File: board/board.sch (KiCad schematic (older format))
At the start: 13 parts

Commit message: Pushing for Kicad reinstall
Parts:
- removed R? (x2): 10k, symbol Device:R_Small
- added C11: 2u2, symbol Device:C_Small
- added C3, C5: 12p, symbol Device:C_Small
- added R1: 47, symbol Device:R_Small_US
- added R2, R3, R6: 0, symbol Device:R_Small_US
- added R4, R5: 10k, symbol Device:R_Small_US
- added U2: MP2359, Package_TO_SOT_SMD:SOT-23-6, symbol custom:MP2359
- added Y1: 16MHz, symbol Device:Crystal_GND24_Small
- gave numbers to parts that had none: 11
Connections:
- net labels added: BUCK_EN, BUCK_IN, BUCK_SW
- wire segments 55 -> 79

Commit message: Small update on power section
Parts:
- added C?: 10u, Capacitor_SMD:C_0603_1608Metric, symbol Device:C_Small
- added C?: 10n, Capacitor_SMD:C_0603_1608Metric, symbol Device:C_Small
- added C? (x2): 2u2, Capacitor_SMD:C_0603_1608Metric, symbol Device:C_Small
- added D?: B5819W, symbol Device:D_Schottky_Small
- added F?: 400mA, symbol Device:Polyfuse_Small
- added FB?: 600 @ 100 MHz, symbol Device:Ferrite_Bead_Small
- added L?: 10u, symbol Device:L_Small
- added Q?: AO3401A, Package_TO_SOT_SMD:SOT-23, symbol Transistor_FET:AO3401A
- added R?: 100k, Resistor_SMD:R_0603_1608Metric, symbol Device:R_Small_US
- added R?: 68k, Resistor_SMD:R_0603_1608Metric, symbol Device:R_Small_US
- added R?: 47k, Resistor_SMD:R_0603_1608Metric, symbol Device:R_Small_US
- added R?: 15k, Resistor_SMD:R_0603_1608Metric, symbol Device:R_Small_US
- added R?: 270, Resistor_SMD:R_0603_1608Metric, symbol Device:R_Small_US
- C1, C11, C8, C9: footprint (none) -> Capacitor_SMD:C_0603_1608Metric
- C10, C12, C2, C3, C4, C5, C6, C7: footprint (none) -> Capacitor_SMD:C_0402_1005Metric
- R1: footprint (none) -> Resistor_SMD:R_0402_1005Metric
- R2, R3, R4, R5, R6: footprint (none) -> Resistor_SMD:R_0603_1608Metric
- U2: symbol custom:MP2359 -> board-rescue:MP2359-custom
- Y1: footprint (none) -> Crystal:Crystal_SMD_3225-4Pin_3.2x2.5mm
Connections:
- net labels added: +12V, BUCK_BST, BUCK_FB
- wire segments 79 -> 111
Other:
- note added: "Under construction"
- moved on the sheet: C12, R4, R5, R6, U3

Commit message: quick push
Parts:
- added D?: D_Zener_Small, symbol Device:D_Zener_Small
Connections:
- net labels added: VCC
- wire segments 111 -> 112
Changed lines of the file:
@@
 $EndComp
 Wire Wire Line
-	7900 3450 8200 3450
+	7900 3450 8000 3450
 $Comp
 L Device:C_Small C?
@@
 Text Notes 7200 7000 0    247  ~ 49
 Under construction
+$Comp
+L Device:D_Zener_Small D?
+U 1 1 6090273B
+P 8000 3350
+F 0 "D?" V 8046 3280 50  0000 R CNN
+F 1 "D_Zener_Small" V 7955 3280 50  0000 R CNN
+F 2 "" V 8000 3350 50  0001 C CNN
+F 3 "~" V 8000 3350 50  0001 C CNN
+	1    8000 3350
+	0    -1   -1   0
+$EndComp
+Connection ~ 8000 3450
+Wire Wire Line
+	8000 3450 8200 3450
+$Comp
+L power:VCC #PWR?
+U 1 1 60903D35
+P 8000 3250
+F 0 "#PWR?" H 8000 3100 50  0001 C CNN
+F 1 "VCC" H 8015 3423 50  0000 C CNN
+F 2 "" H 8000 3250 50  0001 C CNN
+F 3 "" H 8000 3250 50  0001 C CNN
+	1    8000 3250
+	1    0    0    -1
+$EndComp
 $EndSCHEMATC

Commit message: Updated board schematic
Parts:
- removed D?: D_Zener_Small, symbol Device:D_Zener_Small
- removed R2, R3: 0, Resistor_SMD:R_0603_1608Metric, symbol Device:R_Small_US
- added C?: 1u, Capacitor_SMD:C_0402_1005Metric, symbol Device:C_Small
- added C?: 10n, Capacitor_SMD:C_0402_1005Metric, symbol Device:C_Small
- added D1: D_Schottky_Small, symbol Device:D_Schottky_Small
- added FB?: 600 @ 100 MHz, symbol Device:Ferrite_Bead_Small
- added J1: USB_B_Micro, symbol Connector:USB_B_Micro
- added U4: USBLC6-2SC6, Package_TO_SOT_SMD:SOT-23-6, symbol Power_Protection:USBLC6-2SC6
- F1: renamed from F?; value 400mA -> 300mA
- gave numbers to parts that had none: 13
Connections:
- net labels added: USB_CONN_D+, USB_CONN_D-, USB_D+, USB_D-, VBUS
- net labels removed: VCC
- wire segments 112 -> 107
- no-connect marks 0 -> 2
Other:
- note added: "DCDC"
- note added: "Ext. Flash"
- note added: "MCU Decoupling"
- note added: "Power ORing\n"
- note added: "USB"
- moved on the sheet: C11, C13, C14, C15, C16, C3, C5, C8, C9, D2, F1, FB1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

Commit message: Updated board
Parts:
- added D3: POW LED [Gr], LED_SMD:LED_0603_1608Metric, symbol Device:LED_Small
- added R12: 1.5k, Resistor_SMD:R_0603_1608Metric, symbol Device:R_Small_US
- D1, D2: footprint (none) -> Diode_SMD:D_0603_1608Metric
- F1: footprint (none) -> Fuse:Fuse_1206_3216Metric
- FB1, L1: footprint (none) -> Inductor_SMD:L_0603_1608Metric
- FB2: renamed from FB?; footprint (none) -> Inductor_SMD:L_0603_1608Metric
- J1: footprint (none) -> Connector_USB:USB_Micro-B_Amphenol_10103594-0001LF_Horizontal; symbol Connector:USB_B_Micro -> board-rescue:USB_B_Micro-Connector
- gave numbers to parts that had none: 2
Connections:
- net labels added: SPI3_!CS, SPI3_MISO, SPI3_MOSI, SPI3_SCLK, TIM1_CH1
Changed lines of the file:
@@
 $Descr A4 11693 8268
 encoding utf-8
-Sheet 1 1
+Sheet 1 3
 Title ""
 Date ""
@@
 F 0 "F1" V 8400 3550 50  0000 C CNN
 F 1 "300mA" V 8600 3550 50  0000 C CNN
-F 2 "" H 8550 3350 50  0001 L CNN
+F 2 "Fuse:Fuse_1206_3216Metric" H 8550 3350 50  0001 L CNN
 F 3 "~" H 8500 3550 50  0001 C CNN
 	1    8500 3550
@@
 F 0 "FB1" V 8900 3650 50  0000 C CNN
 F 1 "600 @ 100 MHz" V 8650 3750 50  0000 C CNN
-F 2 "" V 8730 3550 50  0001 C CNN
+F 2 "Inductor_SMD:L_0603_1608Metric" V 8730 3550 50  0001 C CNN
 F 3 "~" H 8800 3550 50  0001 C CNN
 	1    8800 3550
@@
 F 0 "D2" V 9700 5500 50  0000 L CNN
 F 1 "B5819W" V 9800 5500 50  0000 L CNN
-F 2 "" V 9750 5850 50  0001 C CNN
+F 2 "Diode_SMD:D_0603_1608Metric" V 9750 5850 50  0001 C CNN
 F 3 "~" V 9750 5850 50  0001 C CNN
 	1    9750 5850
@@
 F 0 "L1" V 10050 5650 50  0000 C CNN
 F 1 "10u" V 9900 5650 50  0000 C CNN
-F 2 "" H 9950 5650 50  0001 C CNN
+F 2 "Inductor_SMD:L_0603_1608Metric" H 9950 5650 50  0001 C CNN
 F 3 "~" H 9950 5650 50  0001 C CNN
 	1    9950 5650
@@
 F 0 "D1" V 8296 3230 50  0000 R CNN
 F 1 "D_Schottky_Small" V 8400 3250 50  0000 R CNN
-F 2 "" V 8250 3300 50  0001 C CNN
+F 2 "Diode_SMD:D_0603_1608Metric" V 8250 3300 50  0001 C CNN
 F 3 "~" V 8250 3300 50  0001 C CNN
 	1    8250 3300
@@
 	8900 3550 9150 3550
 $Comp
-L Connector:USB_B_Micro J1
+L board-rescue:USB_B_Micro-Connector J1
 U 1 1 609103DF
 P 5850 6900
 F 0 "J1" H 5907 7367 50  0000 C CNN
 F 1 "USB_B_Micro" H 5907 7276 50  0000 C CNN
-F 2 "" H 6000 6850 50  0001 C CNN
+F 2 "Connector_USB:USB_Micro-B_Amphenol_10103594-0001LF_Horizontal" H 6000 6850 50  0001 C CNN
 F 3 "~" H 6000 6850 50  0001 C CNN
 	1    5850 6900
@@
 Power ORing\n
 $Comp
-L Device:Ferrite_Bead_Small FB?
+L Device:Ferrite_Bead_Small FB2
 U 1 1 60A20CBB
 P 4050 950
-F 0 "FB?" V 4150 850 50  0000 C CNN
+F 0 "FB2" V 4150 850 50  0000 C CNN
 F 1 "600 @ 100 MHz" V 4250 900 50  0000 C CNN
-F 2 "" V 3980 950 50  0001 C CNN
+F 2 "Inductor_SMD:L_0603_1608Metric" V 3980 950 50  0001 C CNN
 F 3 "~" H 4050 950 50  0001 C CNN
 	1    4050 950
@@
 $EndComp
 $Comp
-L Device:C_Small C?
+L Device:C_Small C17
 U 1 1 60A21654
 P 4350 1050
-F 0 "C?" H 4442 1096 50  0000 L CNN
+F 0 "C17" H 4442 1096 50  0000 L CNN
 F 1 "1u" H 4442 1005 50  0000 L CNN
 F 2 "Capacitor_SMD:C_0402_1005Metric" H 4350 1050 50  0001 C CNN
@@
 $EndComp
 $Comp
-L power:+3V3 #PWR?
+L power:+3V3 #PWR06
 U 1 1 60A21B51
 P 3800 950
-F 0 "#PWR?" H 3800 800 50  0001 C CNN
+F 0 "#PWR06" H 3800 800 50  0001 C CNN
 F 1 "+3V3" H 3815 1123 50  0000 C CNN
 F 2 "" H 3800 950 50  0001 C CNN
@@
 	3950 950  3800 950
 $Comp
-L Device:C_Small C?
+L Device:C_Small C18
 U 1 1 60A25BB7
 P 4750 1050
-F 0 "C?" H 4842 1096 50  0000 L CNN
+F 0 "C18" H 4842 1096 50  0000 L CNN
 F 1 "10n" H 4842 1005 50  0000 L CNN
 F 2 "Capacitor_SMD:C_0402_1005Metric" H 4750 1050 50  0001 C CNN
@@
 $EndComp
 $Comp
-L power:+3.3VA #PWR?
+L power:+3.3VA #PWR08
 U 1 1 60A2600F
 P 4750 850
-F 0 "#PWR?" H 4750 700 50  0001 C CNN
+F 0 "#PWR08" H 4750 700 50  0001 C CNN
 F 1 "+3.3VA" H 4765 1023 50  0000 C CNN
 F 2 "" H 4750 850 50  0001 C CNN
@@
 Connection ~ 4350 950
 $Comp
-L power:GND #PWR?
+L power:GND #PWR07
 U 1 1 60A2FFCD
 P 4350 1150
-F 0 "#PWR?" H 4350 900 50  0001 C CNN
+F 0 "#PWR07" H 4350 900 50  0001 C CNN
 F 1 "GND" H 4355 977 50  0000 C CNN
 F 2 "" H 4350 1150 50  0001 C CNN
@@
 $EndComp
 $Comp
-L power:GND #PWR?
+L power:GND #PWR09
 U 1 1 60A3071E
 P 4750 1150
-F 0 "#PWR?" H 4750 900 50  0001 C CNN
+F 0 "#PWR09" H 4750 900 50  0001 C CNN
 F 1 "GND" H 4755 977 50  0000 C CNN
 F 2 "" H 4750 1150 50  0001 C CNN
@@
 	1    0    0    -1
 $EndComp
+$Sheet
+S 1400 -1250 1250 900
+U 609AD7E8
+F0 "Sheet609AD7E7" 50
+F1 "sensors.sch" 50
+$EndSheet
+Text GLabel 4650 4350 2    50   Input ~ 0
+TIM1_CH1
+$Sheet
+S 2950 -1250 1300 900
+U 609E7CAF
+F0 "Sheet609E7CAE" 50
+F1 "connectors.sch" 50
+$EndSheet
+$Comp
+L power:+3V3 #PWR010
+U 1 1 609E9B02
+P 7400 5500
+F 0 "#PWR010" H 7400 5350 50  0001 C CNN
+F 1 "+3V3" H 7415 5673 50  0000 C CNN
+F 2 "" H 7400 5500 50  0001 C CNN
+F 3 "" H 7400 5500 50  0001 C CNN
+	1    7400 5500
+	1    0    0    -1
+$EndComp
+$Comp
+L power:GND #PWR011
+U 1 1 609EAD75
+P 7400 5900
+F 0 "#PWR011" H 7400 5650 50  0001 C CNN
+F 1 "GND" H 7405 5727 50  0000 C CNN
+F 2 "" H 7400 5900 50  0001 C CNN
+F 3 "" H 7400 5900 50  0001 C CNN
+	1    7400 5900
+	1    0    0    -1
+$EndComp
+$Comp
+L Device:R_Small_US R12
+U 1 1 609EB0ED
+P 7400 5800
+F 0 "R12" V 7300 5850 50  0000 C CNN
+F 1 "1.5k" V 7500 5850 50  0000 C CNN
+F 2 "Resistor_SMD:R_0603_1608Metric" H 7400 5800 50  0001 C CNN
+F 3 "~" H 7400 5800 50  0001 C CNN
+	1    7400 5800
+	-1   0    0    1
+$EndComp
+$Comp
+L Device:LED_Small D3
+U 1 1 609EF0AE
+P 7400 5600
+F 0 "D3" V 7446 5530 50  0000 R CNN
+F 1 "POW LED [Gr]" V 7355 5530 50  0000 R CNN
+F 2 "LED_SMD:LED_0603_1608Metric" V 7400 5600 50  0001 C CNN
+F 3 "~" V 7400 5600 50  0001 C CNN
+	1    7400 5600
+	0    -1   -1   0
+$EndComp
+Text GLabel 4750 4050 2    50   Input ~ 0
+SPI3_!CS
+Text GLabel 4750 3950 2    50   Input ~ 0
+SPI3_SCLK
+Text GLabel 4750 3850 2    50   Input ~ 0
+SPI3_MOSI
+Text GLabel 4750 3750 2    50   Input ~ 0
+SPI3_MISO
 $EndSCHEMATC

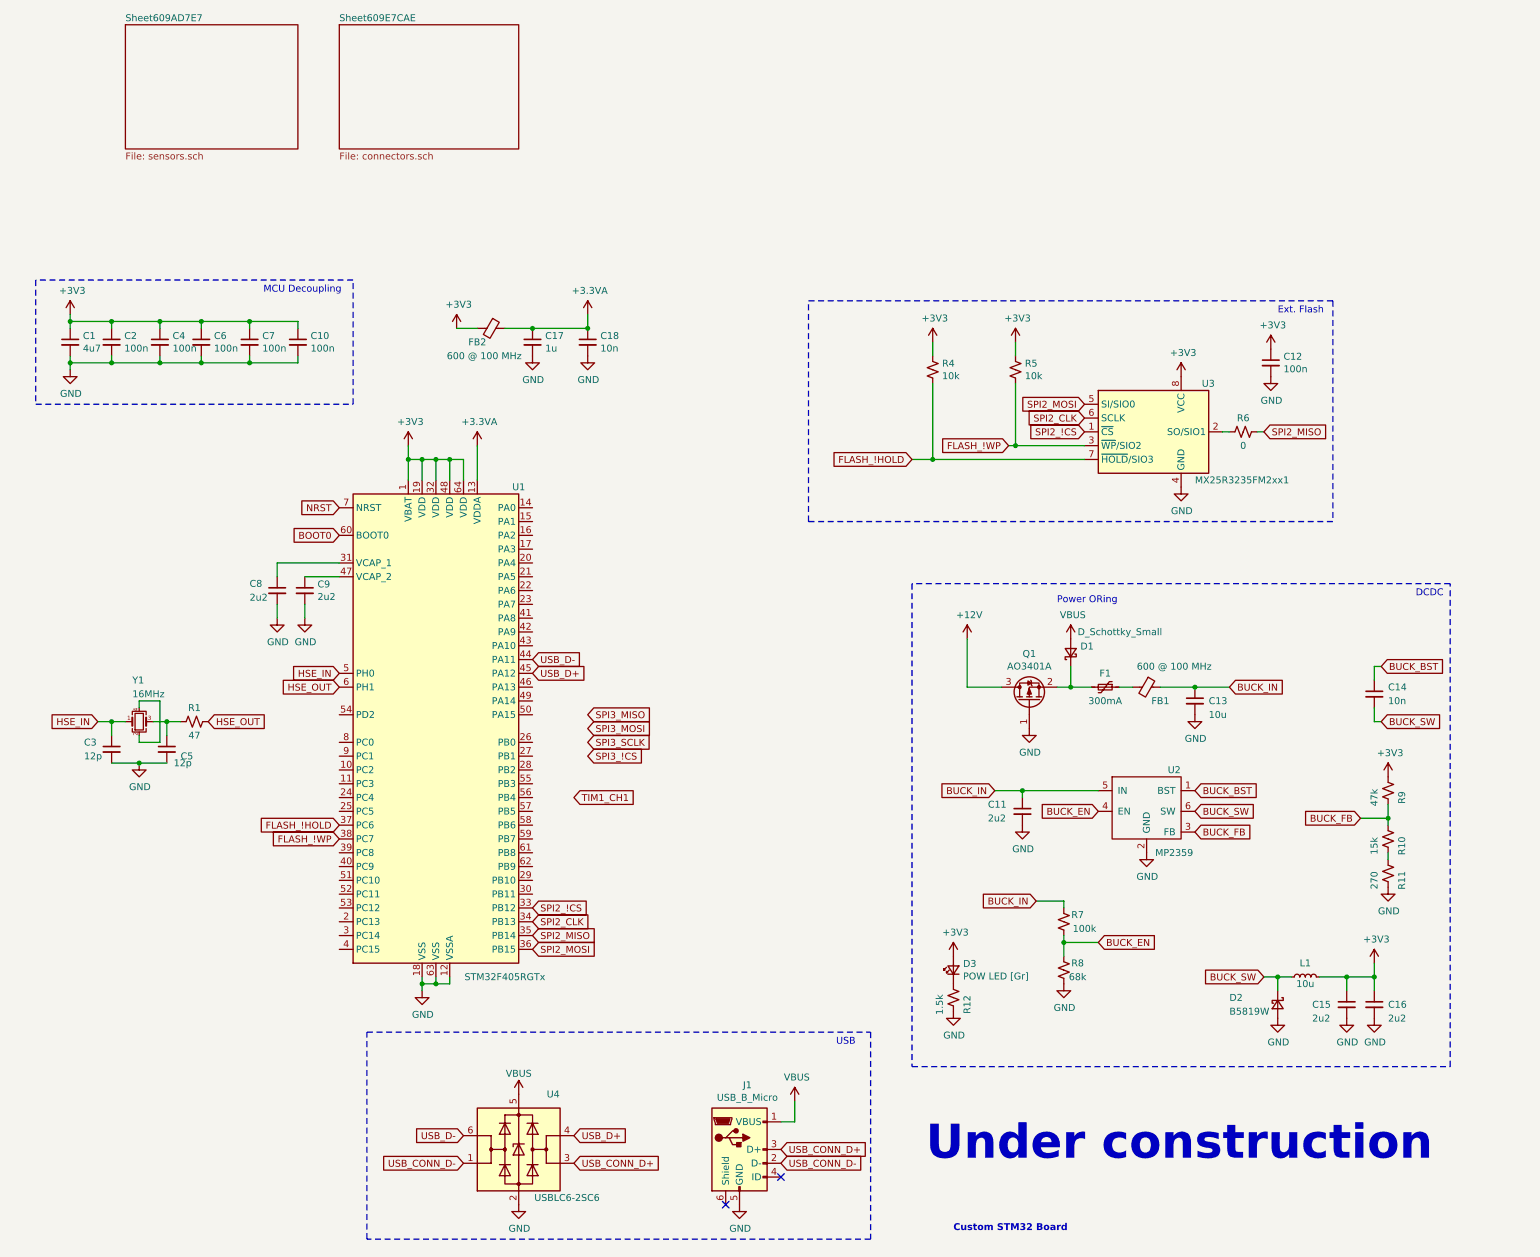
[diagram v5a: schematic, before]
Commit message: Rework on power supply and added pressure sensor
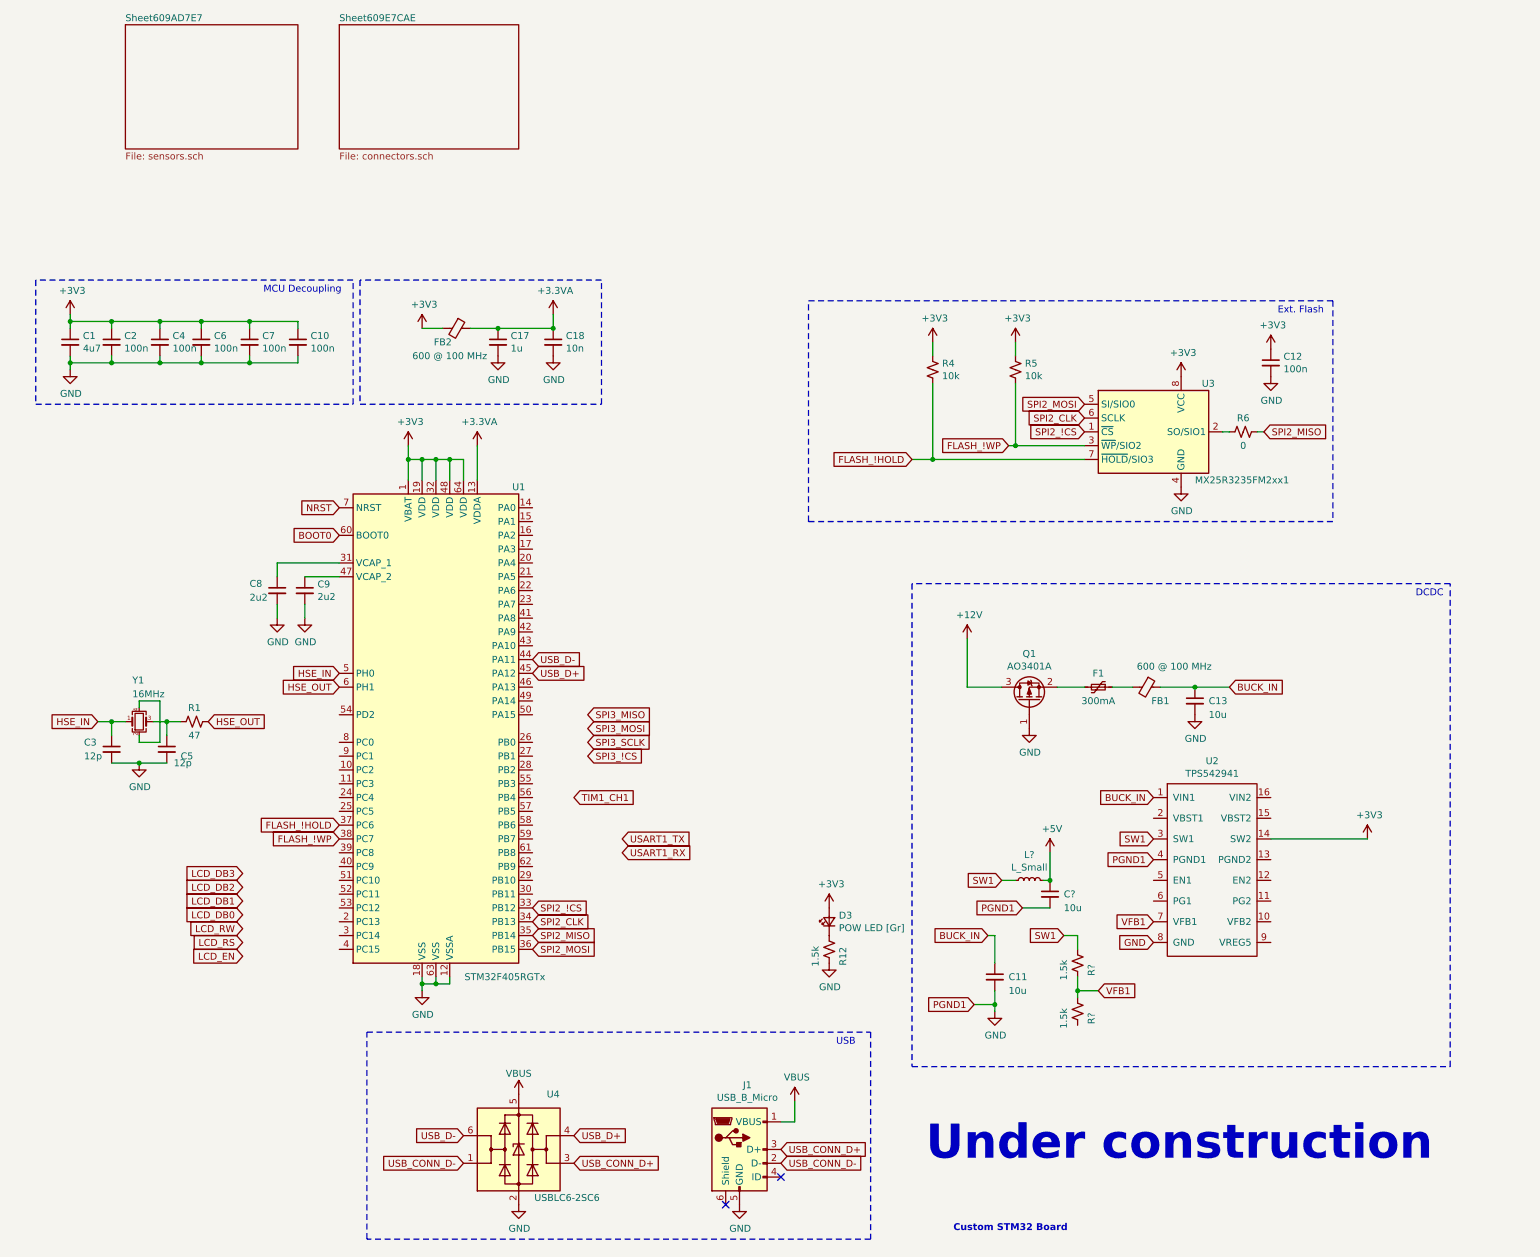
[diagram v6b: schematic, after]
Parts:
- removed C14: 10n, Capacitor_SMD:C_0603_1608Metric, symbol Device:C_Small
- removed C15, C16: 2u2, Capacitor_SMD:C_0603_1608Metric, symbol Device:C_Small
- removed D1: D_Schottky_Small, Diode_SMD:D_0603_1608Metric, symbol Device:D_Schottky_Small
- removed D2: B5819W, Diode_SMD:D_0603_1608Metric, symbol Device:D_Schottky_Small
- removed L1: 10u, Inductor_SMD:L_0603_1608Metric, symbol Device:L_Small
- removed R10: 15k, Resistor_SMD:R_0603_1608Metric, symbol Device:R_Small_US
- removed R11: 270, Resistor_SMD:R_0603_1608Metric, symbol Device:R_Small_US
- removed R7: 100k, Resistor_SMD:R_0603_1608Metric, symbol Device:R_Small_US
- removed R8: 68k, Resistor_SMD:R_0603_1608Metric, symbol Device:R_Small_US
- removed R9: 47k, Resistor_SMD:R_0603_1608Metric, symbol Device:R_Small_US
- removed U2: MP2359, Package_TO_SOT_SMD:SOT-23-6, symbol board-rescue:MP2359-custom
- added C?: 10u, Capacitor_SMD:C_0603_1608Metric, symbol Device:C_Small
- added L?: L_Small, symbol Device:L_Small
- added R? (x2): 1.5k, Resistor_SMD:R_0603_1608Metric, symbol Device:R_Small_US
- added U2: TPS542941, Package_SO:HTSSOP-16-1EP_4.4x5mm_P0.65mm_EP3.4x5mm_Mask2.46x2.31mm_ThermalVias, symbol board-rescue:TPS542941
- C11: value 2u2 -> 10u
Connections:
- net +3V3: now also U2.14 (SW2)
- net BUCK_IN: now also U2.1 (VIN1)
- net GND: now also C?.2, U2.4 (PGND1), U2.8 (GND)
- new net +5V: C?.1, L?.2
- new net SW1: L?.1, R?.2, U2.3 (SW1)
- new net VFB1: R?.1, R?.2, U2.7 (VFB1)
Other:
- note removed: "Power ORing\n"
- moved on the sheet: C17, C18, D3, F1, FB2, R12

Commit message: Update
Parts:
- removed C11: 10u, Capacitor_SMD:C_0603_1608Metric, symbol Device:C_Small
- removed J1: USB_B_Micro, Connector_USB:USB_Micro-B_Amphenol_10103594-0001LF_Horizontal, symbol board-rescue:USB_B_Micro-Connector
- removed U4: USBLC6-2SC6, Package_TO_SOT_SMD:SOT-23-6, symbol Power_Protection:USBLC6-2SC6
- added C13, C21: 22u, Capacitor_SMD:C_0603_1608Metric, symbol Device:C_Small
- added C15, C19: 100n, Capacitor_SMD:C_0603_1608Metric, symbol Device:C_Small
- added C17: 1u, Capacitor_SMD:C_0603_1608Metric, symbol Device:C_Small
- added C20: 10u, Capacitor_SMD:C_0603_1608Metric, symbol Device:C_Small
- added L2: 2u2, Inductor_SMD:L_0603_1608Metric, symbol Device:L_Small
- added R8: 73k2, Resistor_SMD:R_0603_1608Metric, symbol Device:R_Small_US
- added R9: 22k1, Resistor_SMD:R_0603_1608Metric, symbol Device:R_Small_US
- L1: renamed from L?; value L_Small -> 4u7; footprint (none) -> Inductor_SMD:L_0603_1608Metric
- R4: renamed from R?; value 1.5k -> 124k
- R5: renamed from R?; value 1.5k -> 22k1
- gave numbers to parts that had none: 1
- renumbered C17 to C11, C18 to C12, C13 to C16, C12 to C18, C3 to C2, C2 to C3, C5 to C4, C4 to C5, D3 to D1, FB2 to FB1, FB1 to FB2, R12 to R2, R4 to R3, R5 to R6, R6 to R7
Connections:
- net +3V3: now also C21.1, L2.2, R8.2; no longer U2.14 (SW2)
- net +5V: now also L1.1, R4.2, C13.1; no longer C14.1, L1.2
- net BUCK_IN: now also C14.1, U2.16 (VIN2), C20.1
- net GND: now also R5.1, U2.13 (PGND2), C13.2, C17.2, C20.2, C21.2, R9.1
- net SW1: now also L1.2, C15.2; no longer L1.1, R4.2
- net VFB2: now reaches U2.10 (VFB2)
- net VFB2: now also R8.1, R9.2
- net PG2_OUT: now reaches U2.11 (PG2)
- net EN2_IN: now reaches U2.12 (EN2)
- net VBST2: now reaches U2.15 (VBST2)
- net VBST2: now also C19.1
- net VBST1: now reaches U2.2 (VBST1)
- net VBST1: now also C15.1
- net EN1_IN: now reaches U2.5 (EN1)
- net PG1_OUT: now reaches U2.6 (PG1)
- net at U2.9 (VREG5): now also C17.1
- new net SW2: C19.2, L2.1, U2.14 (SW2)
- no-connect marks 2 -> 0
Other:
- note added: "12V +/- 10%"
- note added: "Check values(val, ESR,Vrating, size) + footprint"
- note added: "Fix enables\n"
- note removed: "USB"
- moved on the sheet: C14, C16, C2, C4, C8, C9, D1, F1, FB2, L1, Q1, R1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

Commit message: Generic update
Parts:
- added C24, C25, C26: 100n, Capacitor_SMD:C_0402_1005Metric, symbol Device:C_Small
- added R13: 220, Resistor_SMD:R_0603_1608Metric, symbol Device:R_Small_US
- added R14: 33, Resistor_SMD:R_0603_1608Metric, symbol Device:R_Small_US
- added R15: 10k, Resistor_SMD:R_0603_1608Metric, symbol Device:R_Small_US
- R7: value 0 -> 220
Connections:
- net +3V3: now also C24.1, C25.1, C26.1
- net GND: now also C24.2, C25.2, C26.2, R15.2
- net SPI2_CLK: now also R14.1; no longer U1.34 (PB13)
- net SPI2_MISO: now also U3.2 (SO/SIO1), R15.1; no longer R7.1
- net USART1_RX: now also R13.1
- net USART1_TX: now also R7.1
- net at R7.2: no longer U3.2 (SO/SIO1)
- net PG1_OUT: no longer names the net of U2.6 (PG1)
- net PG2_OUT: no longer names the net of U2.11 (PG2)
- new net: R14.2, U1.34 (PB13)
- no-connect marks 0 -> 2
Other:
- note added: "Analog Decoupling / Filtering\n"
- note added: "Check if this is pull up or down"
- note added: "HSE"
- note added: "MCU"
- note added: "MCU PWR Decoupling\n"
- note added: "UART series resistor\nDecoupling type and values\nLCD ??\nPower LED???"
- note removed: "MCU Decoupling"
- moved on the sheet: C1, C10, C11, C12, C2, C3, C4, C5, C6, C7, D1, FB1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
